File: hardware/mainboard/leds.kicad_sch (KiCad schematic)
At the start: 8 parts

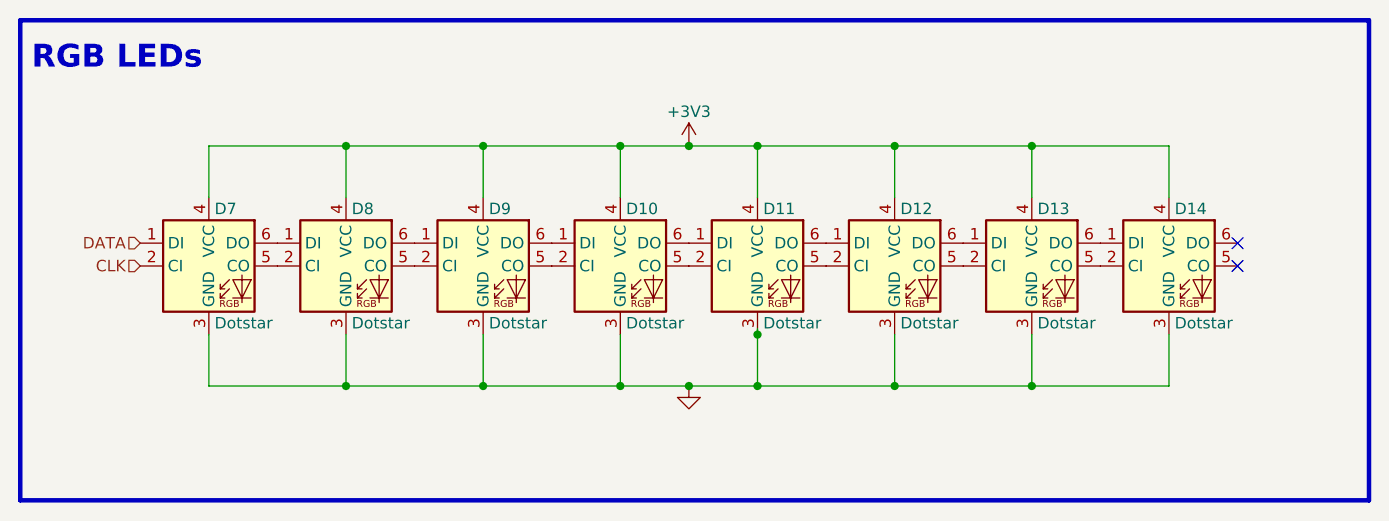
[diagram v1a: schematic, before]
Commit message: hardware: update some labels, fix some fields, re-do fancytext
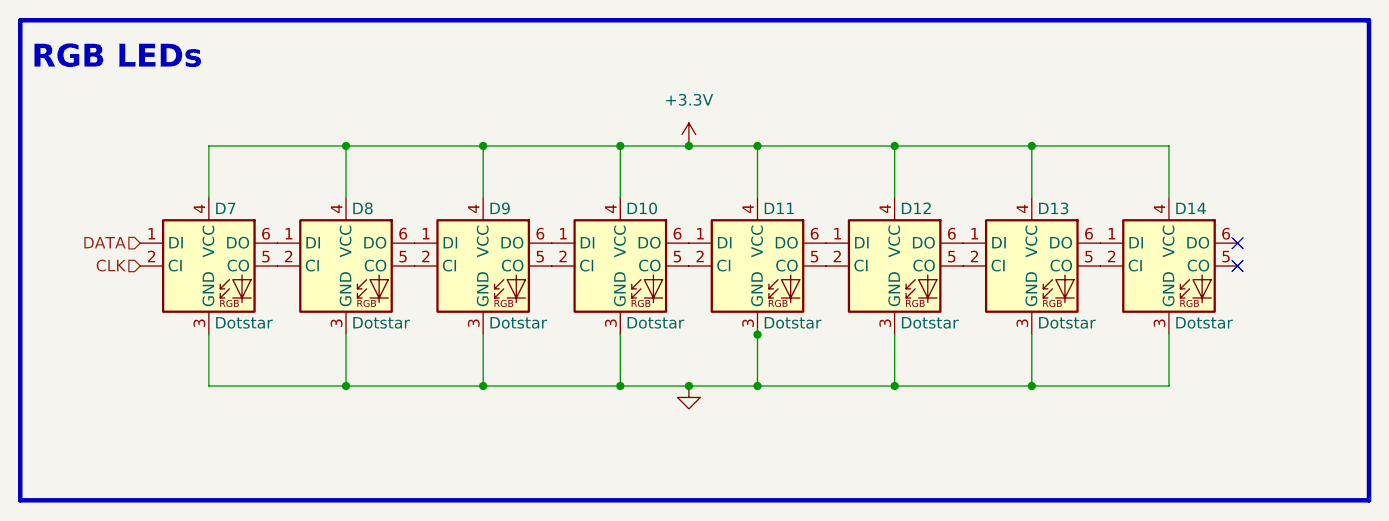
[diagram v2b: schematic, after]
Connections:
- net +3V3 renamed +3.3V
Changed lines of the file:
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@@
   (junction (at 104.775 114.3) (diameter 0) (color 0 0 0 0)
   )
+  (junction (at 142.875 114.3) (diameter 0) (color 0 0 0 0)
+  )
   (junction (at 104.775 87.63) (diameter 0) (color 0 0 0 0)
   )
-  (junction (at 142.875 114.3) (diameter 0) (color 0 0 0 0)
-  )
   (junction (at 150.495 87.63) (diameter 0) (color 0 0 0 0)
   )
@@
   (junction (at 135.255 114.3) (diameter 0) (color 0 0 0 0)
   )
+  (junction (at 142.875 87.63) (diameter 0) (color 0 0 0 0)
+  )
   (junction (at 120.015 114.3) (diameter 0) (color 0 0 0 0)
-  )
-  (junction (at 142.875 87.63) (diameter 0) (color 0 0 0 0)
   )
   (junction (at 150.495 108.585) (diameter 0) (color 0 0 0 0)
@@
     (stroke (width 0.5) (type solid) (color 0 0 0 0))
   )
+  (wire (pts (xy 104.775 87.63) (xy 120.015 87.63))
+    (stroke (width 0) (type default) (color 0 0 0 0))
+  )
   (wire (pts (xy 196.215 114.3) (xy 180.975 114.3))
     (stroke (width 0) (type default) (color 0 0 0 0))
@@
     (stroke (width 0) (type default) (color 0 0 0 0))
   )
+  (wire (pts (xy 142.875 87.63) (xy 150.495 87.63))
+    (stroke (width 0) (type default) (color 0 0 0 0))
+  )
   (wire (pts (xy 89.535 114.3) (xy 89.535 108.585))
     (stroke (width 0) (type default) (color 0 0 0 0))
@@
   )
   (wire (pts (xy 150.495 114.3) (xy 142.875 114.3))
+    (stroke (width 0) (type default) (color 0 0 0 0))
+  )
+  (wire (pts (xy 104.775 87.63) (xy 104.775 93.345))
     (stroke (width 0) (type default) (color 0 0 0 0))
   )
@@
     (stroke (width 0.5) (type solid) (color 0 0 0 0))
   )
+  (wire (pts (xy 89.535 87.63) (xy 89.535 93.345))
+    (stroke (width 0) (type default) (color 0 0 0 0))
+  )
   (wire (pts (xy 196.215 93.345) (xy 196.215 87.63))
     (stroke (width 0) (type default) (color 0 0 0 0))
@@
     (stroke (width 0) (type default) (color 0 0 0 0))
   )
-  (wire (pts (xy 150.495 87.63) (xy 142.875 87.63))
+  (wire (pts (xy 135.255 87.63) (xy 142.875 87.63))
     (stroke (width 0) (type default) (color 0 0 0 0))
   )
@@
     (stroke (width 0) (type default) (color 0 0 0 0))
   )
-  (wire (pts (xy 135.255 87.63) (xy 142.875 87.63))
-    (stroke (width 0) (type default) (color 0 0 0 0))
-  )
   (wire (pts (xy 165.735 108.585) (xy 165.735 114.3))
     (stroke (width 0) (type default) (color 0 0 0 0))
@@
     (stroke (width 0) (type default) (color 0 0 0 0))
   )
-  (wire (pts (xy 104.775 87.63) (xy 104.775 93.345))
-    (stroke (width 0) (type default) (color 0 0 0 0))
-  )
   (wire (pts (xy 150.495 108.585) (xy 150.495 114.3))
     (stroke (width 0) (type default) (color 0 0 0 0))
@@
     (stroke (width 0) (type default) (color 0 0 0 0))
   )
-  (wire (pts (xy 104.775 87.63) (xy 120.015 87.63))
-    (stroke (width 0) (type default) (color 0 0 0 0))
-  )
   (wire (pts (xy 196.215 87.63) (xy 180.975 87.63))
     (stroke (width 0) (type default) (color 0 0 0 0))
@@
   )
   (wire (pts (xy 196.215 108.585) (xy 196.215 114.3))
-    (stroke (width 0) (type default) (color 0 0 0 0))
-  )
-  (wire (pts (xy 89.535 93.345) (xy 89.535 87.63))
     (stroke (width 0) (type default) (color 0 0 0 0))
   )
@@
     (pin "5")
     (pin "6")
+  )
+  (symbol (lib_id "power:+3.3V") (at 142.875 87.63 0) (unit 1)
+    (in_bom yes) (on_board yes) (fields_autoplaced)
+    (property "Reference" "#PWR028" (id 0) (at 142.875 91.44 0)
+      (effects (font (size 1.27 1.27)) hide)
+    )
+    (property "Value" "+3.3V" (id 1) (at 142.875 82.55 0))
+    (property "Footprint" "" (id 2) (at 142.875 87.63 0)
+      (effects (font (size 1.27 1.27)) hide)
+    )
+    (property "Datasheet" "" (id 3) (at 142.875 87.63 0)
+      (effects (font (size 1.27 1.27)) hide)
+    )
+    (pin "1")
   )
   (symbol (lib_id "power:GND") (at 142.875 114.3 0) (unit 1)
@@
       (effects (font (size 1.27 1.27)) hide)
     )
-    (pin "1")
-  )
-  (symbol (lib_id "power:+3V3") (at 142.875 87.63 0) (unit 1)
-    (in_bom yes) (on_board yes)
-    (property "Reference" "#PWR094" (id 0) (at 142.875 91.44 0)
-      (effects (font (size 1.27 1.27)) hide)
-    )
-    (property "Value" "+3V3" (id 1) (at 142.875 83.82 0))
-    (property "Footprint" "" (id 2) (at 142.875 87.63 0)
-      (effects (font (size 1.27 1.27)) hide)
-    )
-    (property "Datasheet" "" (id 3) (at 142.875 87.63 0)
-      (effects (font (size 1.27 1.27)) hide)
-    )
